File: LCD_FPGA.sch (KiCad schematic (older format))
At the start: 2 parts

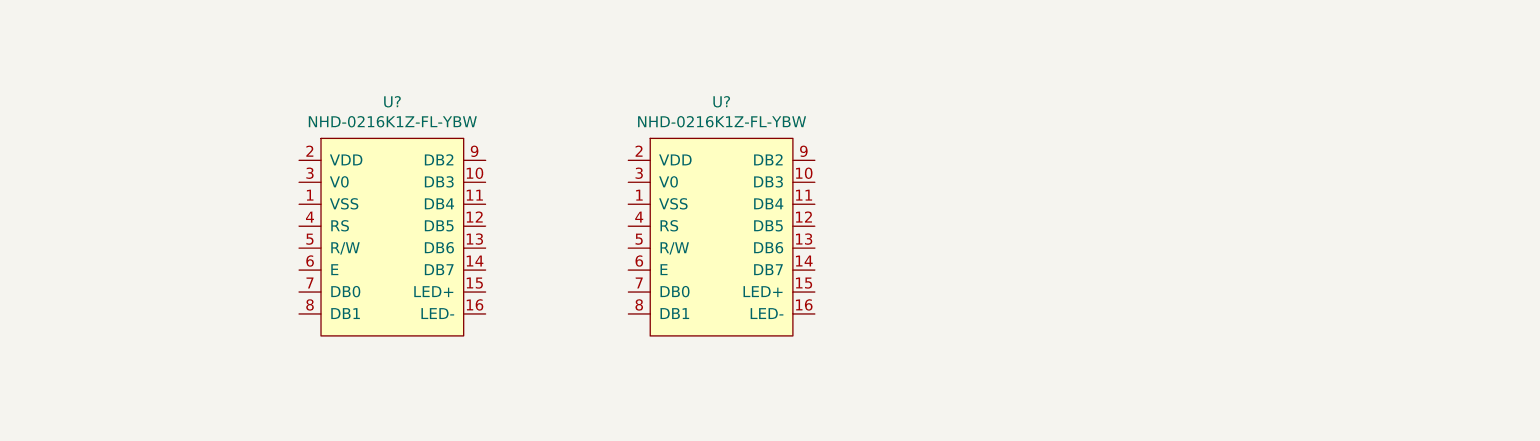
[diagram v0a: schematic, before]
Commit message: 2 LCDs (NHD-0216K1Z-FL-YBW) were connected to the FPGA
Connected the two LCDs (NHD-0216K1Z-FL-YBW) to the FPGA through bank 0
Deleted LCD1 and LCD2 that were connected to the microcontroller
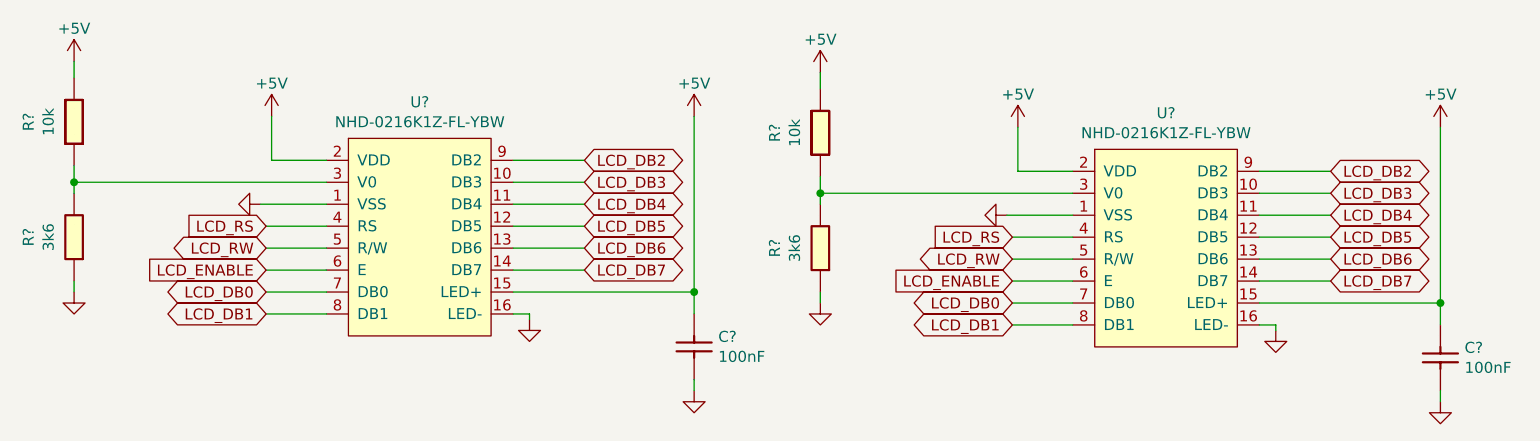
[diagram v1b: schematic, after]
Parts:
- removed U?: NHD-0216K1Z-FL-YBW, symbol OpenVent:NHD-0216K1Z-FL-YBW
- added C? (x2): 100nF_0603_Ceramic_Capacitor,_10%,_X7R,_25V, symbol OpenVent:100nF_0603_Ceramic_Capacitor,_10%,_X7R,_25V
- added R? (x2): 10k_0603_Chip_Resistor,_1%,_0.1W, symbol OpenVent:10k_0603_Chip_Resistor,_1%,_0.1W
- added R? (x2): 3k6_0603_Chip_Resistor,_1%,_0.1W, symbol OpenVent:3k6_0603_Chip_Resistor,_1%,_0.1W
- added U?: NHD-0216K1Z-FL-YBW, symbol OpenVent:NHD-0216K1Z-FL-YBW
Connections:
- net GND: now reaches U?.1 (VSS)
- net GND: now also U?.16 (LED-), C?.2, C?.2, R?.1, R?.1, U?.1 (VSS), U?.16 (LED-)
- net LCD_DB3: now reaches U?.10 (DB3)
- net LCD_DB3: now also U?.10 (DB3)
- net LCD_DB4: now reaches U?.11 (DB4)
- net LCD_DB4: now also U?.11 (DB4)
- net LCD_DB5: now reaches U?.12 (DB5)
- net LCD_DB5: now also U?.12 (DB5)
- net LCD_DB6: now reaches U?.13 (DB6)
- net LCD_DB6: now also U?.13 (DB6)
- net LCD_DB7: now reaches U?.14 (DB7)
- net LCD_DB7: now also U?.14 (DB7)
- net +5V: now reaches U?.15 (LED+)
- net +5V: now also U?.2 (VDD), C?.1, C?.1, R?.2, R?.2, U?.15 (LED+), U?.2 (VDD)
- net at U?.3 (V0): now also R?.1, R?.2
- net LCD_RS: now reaches U?.4 (RS)
- net LCD_RS: now also U?.4 (RS)
- net LCD_RW: now reaches U?.5 (R/W)
- net LCD_RW: now also U?.5 (R/W)
- net LCD_ENABLE: now reaches U?.6 (E)
- net LCD_ENABLE: now also U?.6 (E)
- net LCD_DB0: now reaches U?.7 (DB0)
- net LCD_DB0: now also U?.7 (DB0)
- net LCD_DB1: now reaches U?.8 (DB1)
- net LCD_DB1: now also U?.8 (DB1)
- net LCD_DB2: now reaches U?.9 (DB2)
- net LCD_DB2: now also U?.9 (DB2)
- new net: R?.1, R?.2, U?.3 (V0)
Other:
- moved on the sheet: U?

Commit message: More fixing up of the FPGA symbols, lashed up the sigma delta A/D converter circuitry.  Fixed up the LCD page.  Two displays, two separate enables needed here folks.  FPGA I/O banks power supplies' needs another looking at.  Still lots of stuff to clean up here...
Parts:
- removed U? (x2): NHD-0216K1Z-FL-YBW, symbol OpenVent:NHD-0216K1Z-FL-YBW
- added LCD1, LCD2: LCD_MOD_32DIG_16X2_TRANS_YLW_GRN, symbol OpenVent:LCD_MOD_32DIG_16X2_TRANS_YLW_GRN
- gave numbers to parts that had none: 6
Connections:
- net +5V: now also LCD1.15 (A), LCD1.2 (VDD), LCD2.15 (A), LCD2.2 (VDD)
- net GND: now also R34.2, R82.2, LCD1.1 (GND), LCD1.16 (C), LCD2.1 (GND), LCD2.16 (C); no longer R34.1, R82.1
- net LCD_DB0: now also LCD1.7 (D0), LCD2.7 (D0)
- net LCD_DB1: now also LCD1.8 (D1), LCD2.8 (D1)
- net LCD_DB2: now also LCD1.9 (D2), LCD2.9 (D2)
- net LCD_DB3: now also LCD1.10 (D3), LCD2.10 (D3)
- net LCD_DB4: now also LCD1.11 (D4), LCD2.11 (D4)
- net LCD_DB5: now also LCD1.12 (D5), LCD2.12 (D5)
- net LCD_DB6: now also LCD1.13 (D6), LCD2.13 (D6)
- net LCD_DB7: now also LCD1.14 (D7), LCD2.14 (D7)
- net LCD_RS: now also LCD1.4 (RS), LCD2.4 (RS)
- net LCD_RW: now also LCD1.5 (R/~W), LCD2.5 (R/~W)
- net at R84.1: now also R82.1, LCD1.3 (VO); no longer R82.2
- net at R83.1: now also R34.1, LCD2.3 (VO); no longer R34.2
- new net LCD_A_ENABLE: LCD1.6 (E)
- new net LCD_B_ENABLE: LCD2.6 (E)
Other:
- moved on the sheet: C13, C2, R34, R82, R83, R84

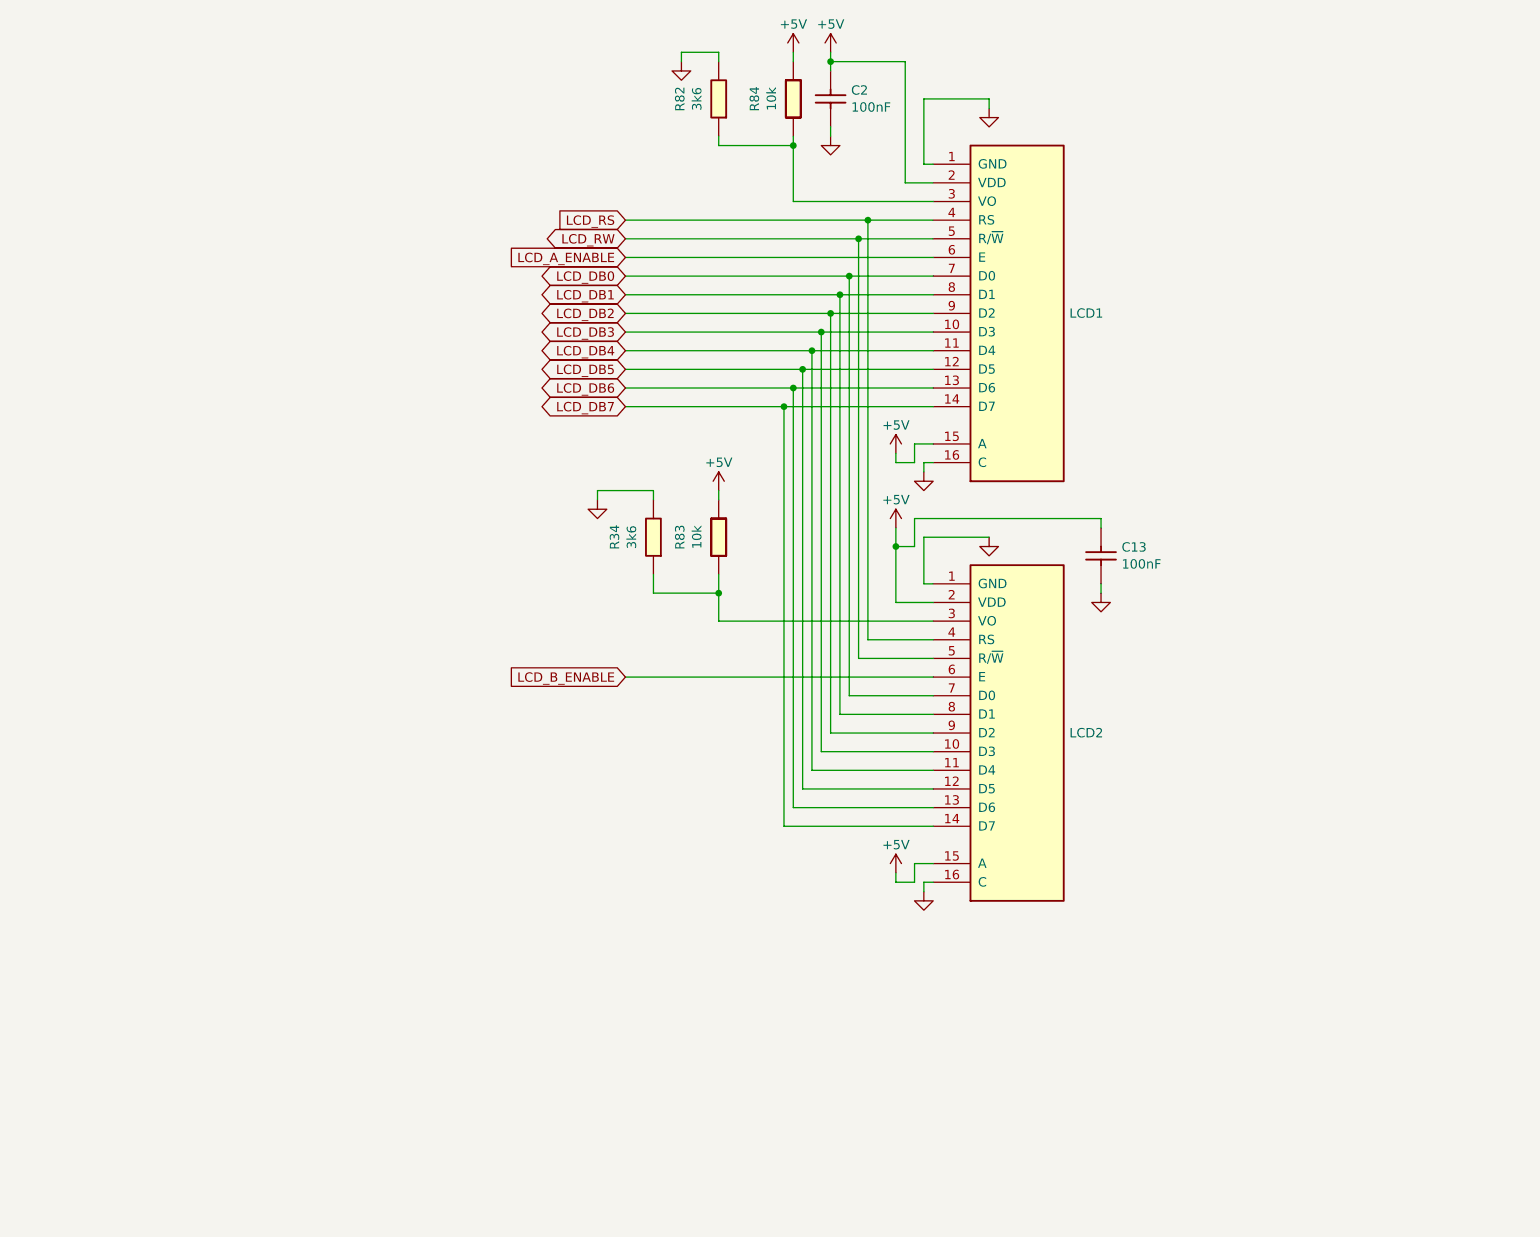
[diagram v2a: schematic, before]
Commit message: Two voltage level translators have been added
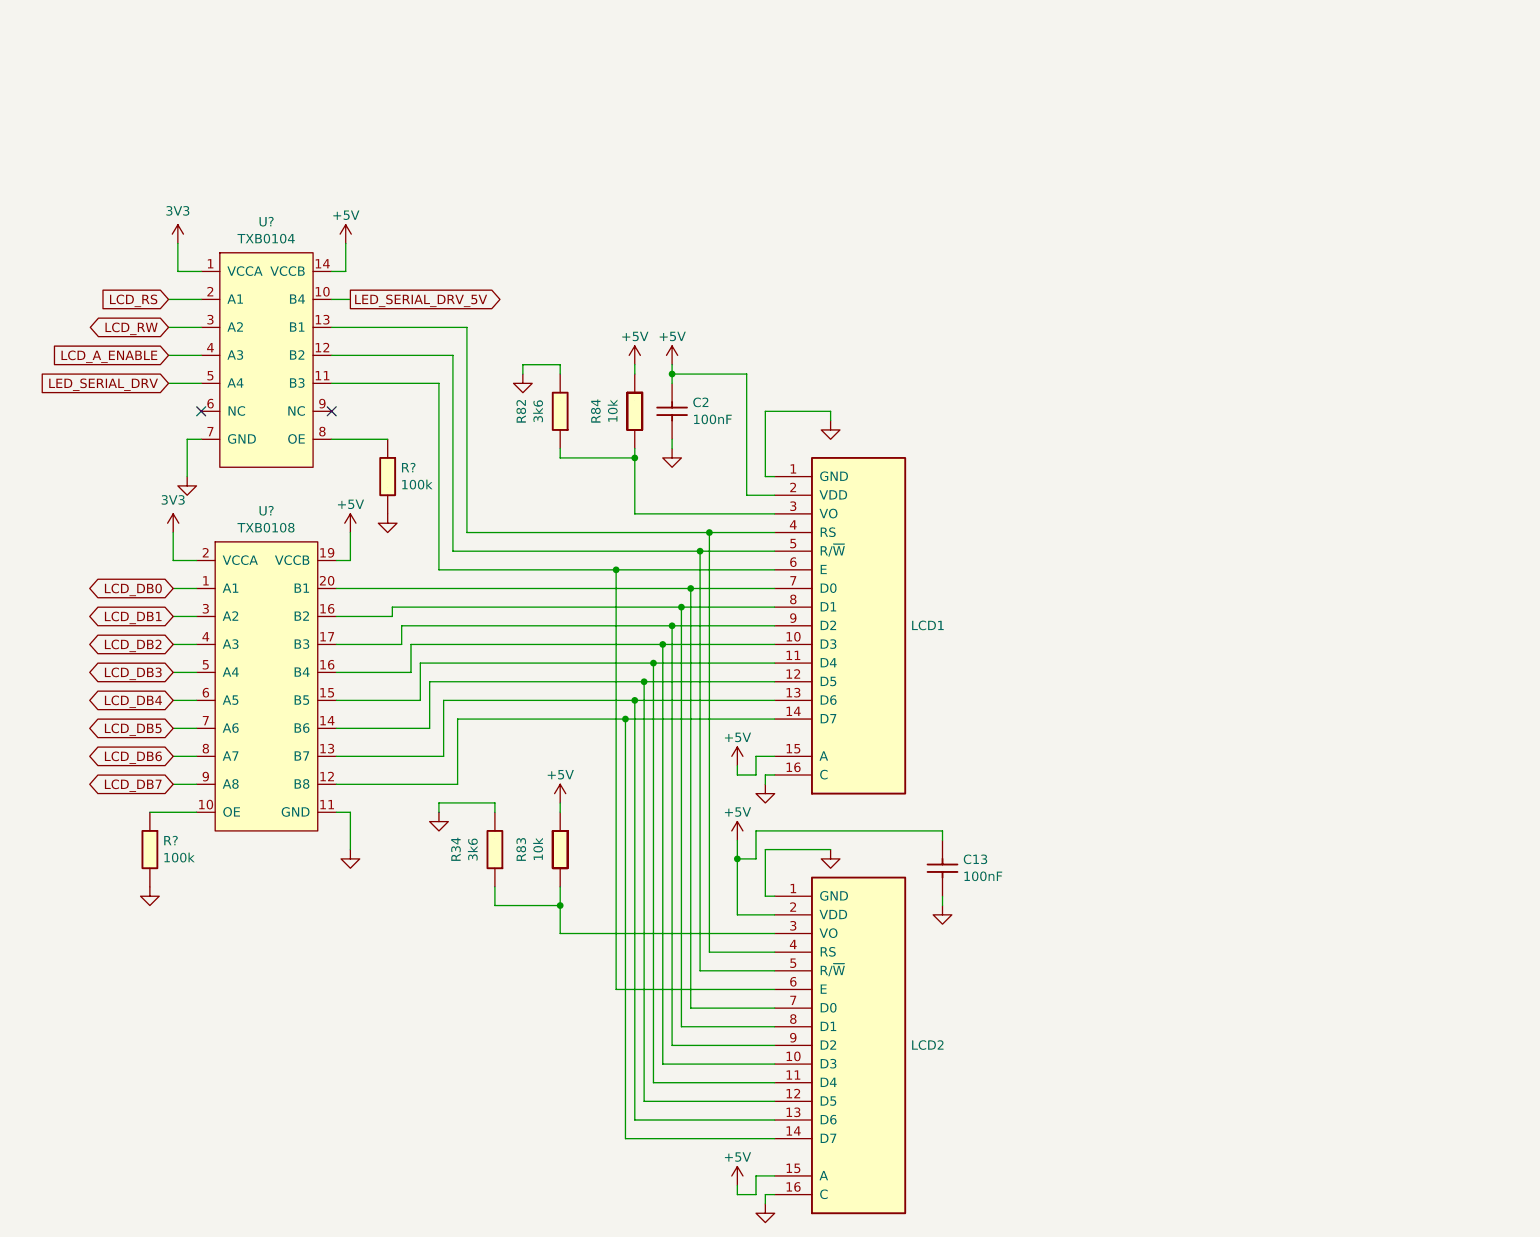
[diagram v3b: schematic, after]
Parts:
- added R? (x2): 100K_0603_Chip_Resistor,_1%,_0.1W, symbol OpenVent:100K_0603_Chip_Resistor,_1%,_0.1W
- added U?: TXB0108, symbol OpenVent:TXB0108
- added U?: TXB0104, symbol OpenVent:TXB0104
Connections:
- net +5V: now also U?.14 (VCCB), U?.19 (VCCB)
- net GND: now also R?.2, R?.2, U?.11 (GND), U?.7 (GND)
- net LCD_A_ENABLE: now also U?.4 (A3); no longer LCD1.6 (E)
- net LCD_DB0: now also U?.1 (A1); no longer LCD1.7 (D0), LCD2.7 (D0)
- net LCD_DB1: now also U?.3 (A2); no longer LCD1.8 (D1), LCD2.8 (D1)
- net LCD_DB2: now also U?.4 (A3); no longer LCD1.9 (D2), LCD2.9 (D2)
- net LCD_DB3: now also U?.5 (A4); no longer LCD1.10 (D3), LCD2.10 (D3)
- net LCD_DB4: now also U?.6 (A5); no longer LCD1.11 (D4), LCD2.11 (D4)
- net LCD_DB5: now also U?.7 (A6); no longer LCD1.12 (D5), LCD2.12 (D5)
- net LCD_DB6: now also U?.8 (A7); no longer LCD1.13 (D6), LCD2.13 (D6)
- net LCD_DB7: now also U?.9 (A8); no longer LCD1.14 (D7), LCD2.14 (D7)
- net LCD_RS: now also U?.2 (A1); no longer LCD1.4 (RS), LCD2.4 (RS)
- net LCD_RW: now also U?.3 (A2); no longer LCD1.5 (R/~W), LCD2.5 (R/~W)
- net LCD_B_ENABLE: no longer names the net of LCD2.6 (E)
- net LCD_B_ENABLE: now also LCD1.6 (E), U?.11 (B3)
- new net: R?.1, U?.10 (OE)
- new net: LCD1.14 (D7), LCD2.14 (D7), U?.12 (B8)
- new net: LCD1.13 (D6), LCD2.13 (D6), U?.13 (B7)
- new net: LCD1.12 (D5), LCD2.12 (D5), U?.14 (B6)
- new net: LCD1.11 (D4), LCD2.11 (D4), U?.15 (B5)
- new net: LCD1.10 (D3), LCD2.10 (D3), U?.16 (B4)
- new net: LCD1.8 (D1), LCD2.8 (D1), U?.16 (B4)
- new net: LCD1.9 (D2), LCD2.9 (D2), U?.17 (B3)
- new net: LCD1.7 (D0), LCD2.7 (D0), U?.20 (B1)
- new net: LCD1.5 (R/~W), LCD2.5 (R/~W), U?.12 (B2)
- new net: LCD1.4 (RS), LCD2.4 (RS), U?.13 (B1)
- new net: R?.1, U?.8 (OE)
- new net +3V3: U?.1 (VCCA), U?.2 (VCCA)
- new net LED_SERIAL_DRV: U?.5 (A4)
- new net LED_SERIAL_DRV_5V: U?.10 (B4)
- no-connect marks 0 -> 2
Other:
- moved on the sheet: C13, C2, LCD1, LCD2, R34, R82, R83, R84
